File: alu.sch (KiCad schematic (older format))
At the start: 124 parts, among them U1 C96ABC, U10 74LS32, U11 74LS86, U12 74LS86, U13 74LS283, U14 74LS283, U15 74LS253, U16 74LS253, U17 74LS253, U18 74LS253, U2 74ACT04, U3 74ACT04, U4 74ACT158, U5 74ACT158, U6 74ACT158, U7 74LS08, U8 74LS08, U9 74LS32

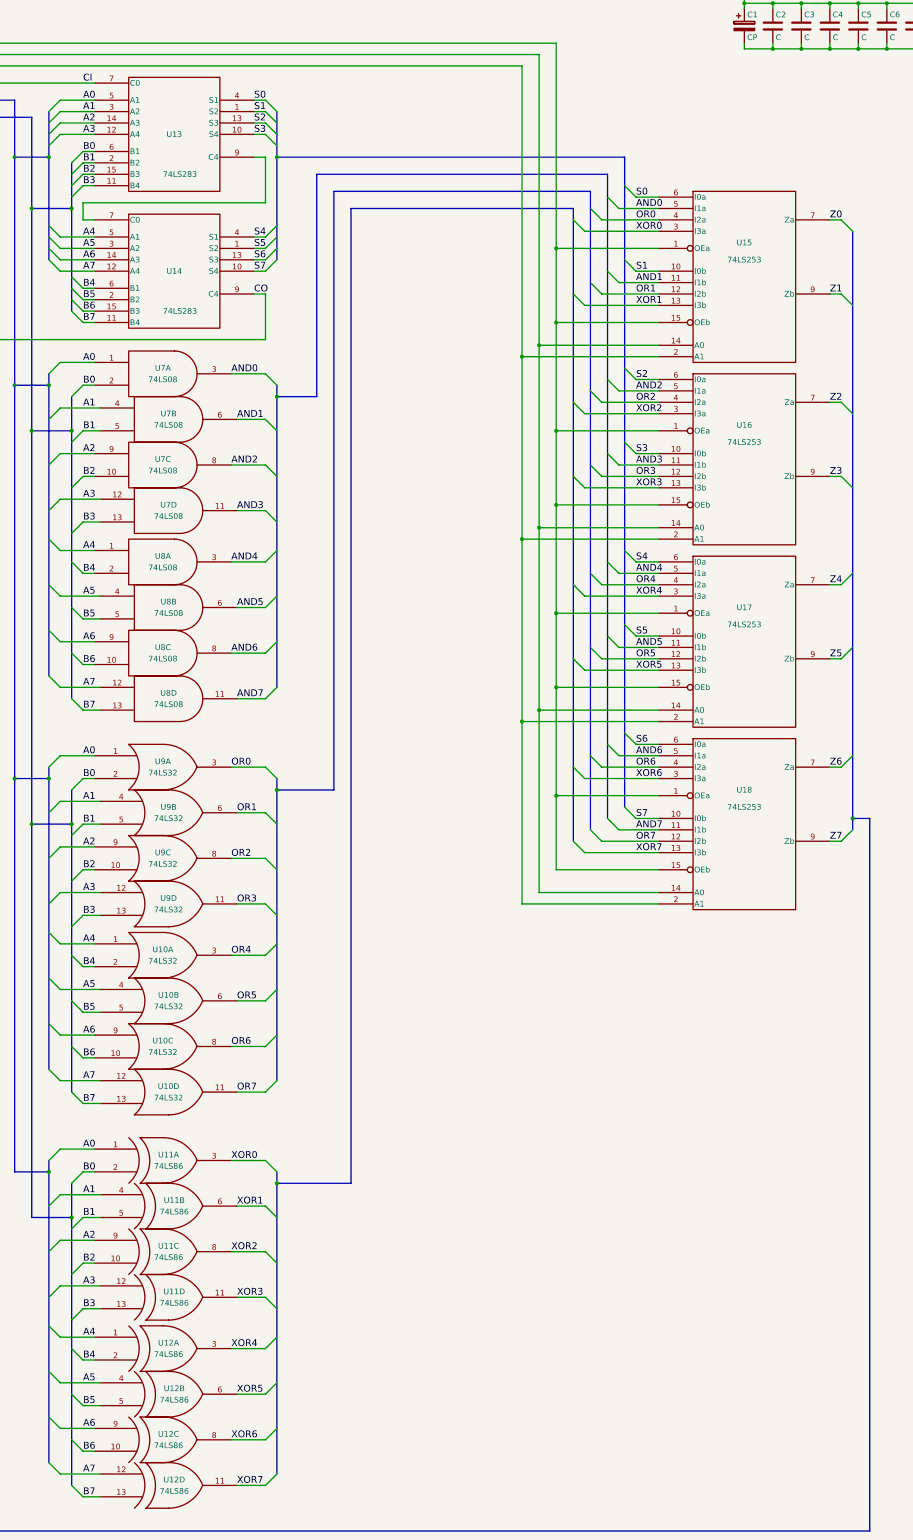
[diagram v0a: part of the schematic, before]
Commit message: component placement
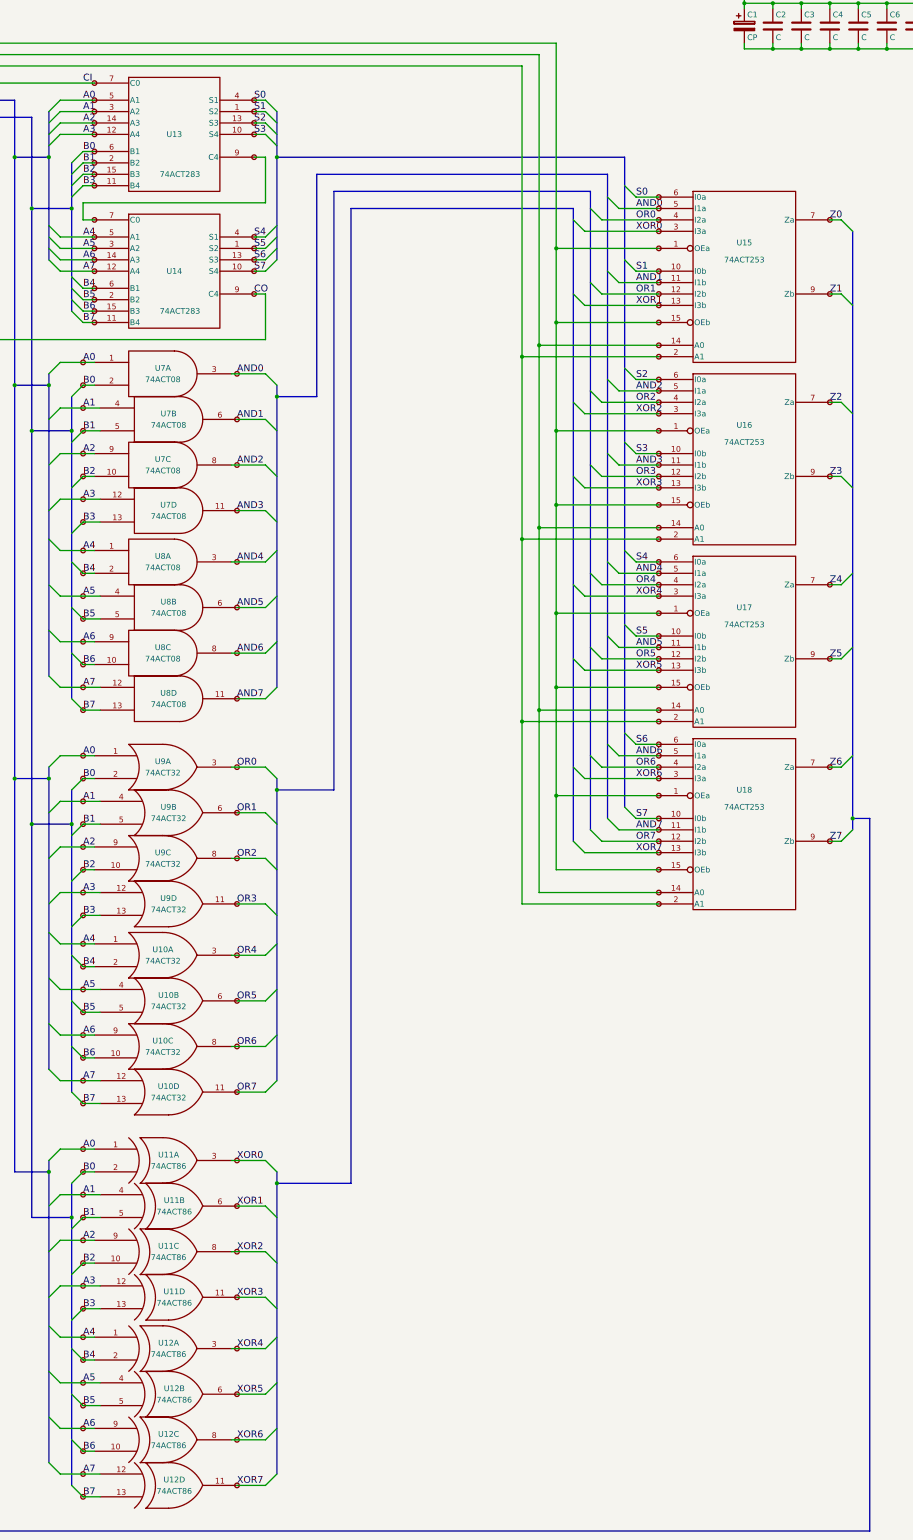
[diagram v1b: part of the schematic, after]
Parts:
- added LED100, LED101, LED102, LED103, LED104, LED105, LED106, LED107, LED108, LED109, LED110, LED111, LED112, LED113, LED114, LED115, LED116, LED117, LED118, LED119, LED120, LED121, LED122, LED123, LED124, LED125, LED126, LED127, LED128, LED129, LED130, LED131, LED132, LED133, LED134, LED135, LED136, LED137, LED138, LED139, LED140, LED141, LED142, LED143, LED144, LED145, LED146, LED147, LED148, LED149, LED150, LED151, LED152, LED153, LED154, LED155, LED156, LED157, LED158, LED159, LED160, LED161, LED162, LED163, LED164, LED165, LED166, LED167, LED168, LED169, LED170, LED171, LED172, LED173, LED174, LED175, LED176, LED177, LED178, LED179, LED180, LED181, LED182, LED183, LED184, LED185, LED186, LED187, LED188, LED189, LED190, LED191, LED192, LED193, LED194, LED195, LED196, LED197, LED198, LED199, LED200, LED201, LED202, LED203, LED204, LED205, LED206, LED207, LED208, LED209, LED210, LED211, LED212, LED213, LED214, LED215, LED216, LED217, LED218, LED219, LED220, LED221, LED222, LED223, LED224, LED225, LED226, LED227, LED228, LED229, LED230, LED231, LED232, LED233, LED234, LED235, LED236, LED237, LED238, LED239, LED240, LED241, LED242, LED243, LED244, LED89, LED90, LED91, LED92, LED93, LED94, LED95, LED96, LED97, LED98, LED99: DEBUG_LED, LEDs:LED-3MM, symbol DEBUG_LED
- U10, U9: value 74LS32 -> 74ACT32
- U11, U12: value 74LS86 -> 74ACT86
- U13, U14: value 74LS283 -> 74ACT283
- U15, U16, U17, U18: value 74LS253 -> 74ACT253
- U7, U8: value 74LS08 -> 74ACT08
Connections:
- net A0: now also LED113.2, LED137.2, LED162.2, LED89.2
- net A1: now also LED115.2, LED139.2, LED163.2, LED91.2
- net A2: now also LED117.2, LED141.2, LED164.2, LED93.2
- net A3: now also LED119.2, LED143.2, LED165.2, LED95.2
- net A4: now also LED121.2, LED145.2, LED171.2, LED97.2
- net A5: now also LED123.2, LED147.2, LED172.2, LED99.2
- net A6: now also LED101.2, LED125.2, LED149.2, LED173.2
- net A7: now also LED103.2, LED127.2, LED151.2, LED174.2
- net AND0: now also LED105.2, LED190.2
- net AND1: now also LED106.2, LED195.2
- net AND2: now also LED107.2, LED202.2
- net AND3: now also LED108.2, LED207.2
- net AND4: now also LED109.2, LED214.2
- net AND5: now also LED110.2, LED219.2
- net AND6: now also LED111.2, LED226.2
- net AND7: now also LED112.2, LED231.2
- net B0: now also LED114.2, LED138.2, LED166.2, LED90.2
- net B1: now also LED116.2, LED140.2, LED167.2, LED92.2
- net B2: now also LED118.2, LED142.2, LED168.2, LED94.2
- net B3: now also LED120.2, LED144.2, LED169.2, LED96.2
- net B4: now also LED122.2, LED146.2, LED175.2, LED98.2
- net B5: now also LED100.2, LED124.2, LED148.2, LED176.2
- net B6: now also LED102.2, LED126.2, LED150.2, LED177.2
- net B7: now also LED104.2, LED128.2, LED152.2, LED178.2
- net CI: now also LED161.2
- net CO: now also LED188.2
- net GND: now also LED100.1 (GND), LED101.1 (GND), LED102.1 (GND), LED103.1 (GND), LED104.1 (GND), LED105.1 (GND), LED106.1 (GND), LED107.1 (GND), LED108.1 (GND), LED109.1 (GND), LED110.1 (GND), LED111.1 (GND), LED112.1 (GND), LED113.1 (GND), LED114.1 (GND), LED115.1 (GND), LED116.1 (GND), LED117.1 (GND), LED118.1 (GND), LED119.1 (GND), LED120.1 (GND), LED121.1 (GND), LED122.1 (GND), LED123.1 (GND), LED124.1 (GND), LED125.1 (GND), LED126.1 (GND), LED127.1 (GND), LED128.1 (GND), LED129.1 (GND), LED130.1 (GND), LED131.1 (GND), LED132.1 (GND), LED133.1 (GND), LED134.1 (GND), LED135.1 (GND), LED136.1 (GND), LED137.1 (GND), LED138.1 (GND), LED139.1 (GND), LED140.1 (GND), LED141.1 (GND), LED142.1 (GND), LED143.1 (GND), LED144.1 (GND), LED145.1 (GND), LED146.1 (GND), LED147.1 (GND), LED148.1 (GND), LED149.1 (GND), LED150.1 (GND), LED151.1 (GND), LED152.1 (GND), LED153.1 (GND), LED154.1 (GND), LED155.1 (GND), LED156.1 (GND), LED157.1 (GND), LED158.1 (GND), LED159.1 (GND), LED160.1 (GND), LED161.1 (GND), LED162.1 (GND), LED163.1 (GND), LED164.1 (GND), LED165.1 (GND), LED166.1 (GND), LED167.1 (GND), LED168.1 (GND), LED169.1 (GND), LED170.1 (GND), LED171.1 (GND), LED172.1 (GND), LED173.1 (GND), LED174.1 (GND), LED175.1 (GND), LED176.1 (GND), LED177.1 (GND), LED178.1 (GND), LED179.1 (GND), LED180.1 (GND), LED181.1 (GND), LED182.1 (GND), LED183.1 (GND), LED184.1 (GND), LED185.1 (GND), LED186.1 (GND), LED187.1 (GND), LED188.1 (GND), LED189.1 (GND), LED190.1 (GND), LED191.1 (GND), LED192.1 (GND), LED193.1 (GND), LED194.1 (GND), LED195.1 (GND), LED196.1 (GND), LED197.1 (GND), LED198.1 (GND), LED199.1 (GND), LED200.1 (GND), LED201.1 (GND), LED202.1 (GND), LED203.1 (GND), LED204.1 (GND), LED205.1 (GND), LED206.1 (GND), LED207.1 (GND), LED208.1 (GND), LED209.1 (GND), LED210.1 (GND), LED211.1 (GND), LED212.1 (GND), LED213.1 (GND), LED214.1 (GND), LED215.1 (GND), LED216.1 (GND), LED217.1 (GND), LED218.1 (GND), LED219.1 (GND), LED220.1 (GND), LED221.1 (GND), LED222.1 (GND), LED223.1 (GND), LED224.1 (GND), LED225.1 (GND), LED226.1 (GND), LED227.1 (GND), LED228.1 (GND), LED229.1 (GND), LED230.1 (GND), LED231.1 (GND), LED232.1 (GND), LED233.1 (GND), LED234.1 (GND), LED235.1 (GND), LED236.1 (GND), LED237.1 (GND), LED238.1 (GND), LED239.1 (GND), LED240.1 (GND), LED241.1 (GND), LED242.1 (GND), LED243.1 (GND), LED244.1 (GND), LED89.1 (GND), LED90.1 (GND), LED91.1 (GND), LED92.1 (GND), LED93.1 (GND), LED94.1 (GND), LED95.1 (GND), LED96.1 (GND), LED97.1 (GND), LED98.1 (GND), LED99.1 (GND)
- net OR0: now also LED129.2, LED191.2
- net OR1: now also LED130.2, LED196.2
- net OR2: now also LED131.2, LED203.2
- net OR3: now also LED132.2, LED208.2
- net OR4: now also LED133.2, LED215.2
- net OR5: now also LED134.2, LED220.2
- net OR6: now also LED135.2, LED227.2
- net OR7: now also LED136.2, LED232.2
- net S0: now also LED179.2, LED189.2
- net S1: now also LED180.2, LED194.2
- net S2: now also LED181.2, LED201.2
- net S3: now also LED182.2, LED206.2
- net S4: now also LED184.2, LED213.2
- net S5: now also LED185.2, LED218.2
- net S6: now also LED186.2, LED225.2
- net S7: now also LED187.2, LED230.2
- net XOR0: now also LED153.2, LED192.2
- net XOR1: now also LED154.2, LED197.2
- net XOR2: now also LED155.2, LED204.2
- net XOR3: now also LED156.2, LED209.2
- net XOR4: now also LED157.2, LED216.2
- net XOR5: now also LED158.2, LED221.2
- net XOR6: now also LED159.2, LED228.2
- net XOR7: now also LED160.2, LED233.2
- net Y0: now also LED199.2, LED211.2, LED223.2, LED235.2
- net Y1: now also LED200.2, LED212.2, LED224.2, LED236.2
- net Z0: now also LED237.2
- net Z1: now also LED238.2
- net Z2: now also LED239.2
- net Z3: now also LED240.2
- net Z4: now also LED241.2
- net Z5: now also LED242.2
- net Z6: now also LED243.2
- net Z7: now also LED244.2
- net ~OE: now also LED193.2, LED198.2, LED205.2, LED210.2, LED217.2, LED222.2, LED229.2, LED234.2
- net at U13.9 (C4), U14.7 (C0): now also LED170.2, LED183.2

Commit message: pcb routing
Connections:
- net A0: now also U1.C26 (26C); no longer U1.C27 (27C)
- net A1: now also U1.C25 (25C); no longer U1.C26 (26C)
- net A2: now also U1.C24 (24C); no longer U1.C25 (25C)
- net A3: now also U1.C23 (23C); no longer U1.C24 (24C)
- net A4: now also U1.C22 (22C); no longer U1.C23 (23C)
- net A5: now also U1.C21 (21C); no longer U1.C22 (22C)
- net A6: now also U1.C20 (20C); no longer U1.C21 (21C)
- net A7: now also U1.C19 (19C); no longer U1.C20 (20C)
- net BFF: now also U1.B27 (27B); no longer U1.B28 (28B)
- net BX0: now also U1.C18 (18C); no longer U1.C19 (19C)
- net BX1: now also U1.C17 (17C); no longer U1.C18 (18C)
- net BX2: now also U1.C16 (16C); no longer U1.C17 (17C)
- net BX3: now also U1.C15 (15C); no longer U1.C16 (16C)
- net BX4: now also U1.C14 (14C); no longer U1.C15 (15C)
- net BX5: now also U1.C13 (13C); no longer U1.C14 (14C)
- net BX6: now also U1.C12 (12C); no longer U1.C13 (13C)
- net BX7: now also U1.C11 (11C); no longer U1.C12 (12C)
- net CIX: now also U1.C10 (10C); no longer U1.C11 (11C)
- net COX: now also U1.C1 (1C); no longer U1.C2 (2C)
- net CSET: now also U1.B28 (28B); no longer U1.B29 (29B)
- net GND: now also U1.A31 (31A), U1.B31 (31B), U1.C31 (31C); no longer U1.A1 (1A), U1.B1 (1B), U1.C1 (1C)
- net Y0: now also U1.C29 (29C); no longer U1.C30 (30C)
- net Y1: now also U1.C28 (28C); no longer U1.C29 (29C)
- net Z0: now also U1.C9 (9C); no longer U1.C10 (10C)
- net Z1: now also U1.C8 (8C); no longer U1.C9 (9C)
- net Z2: now also U1.C7 (7C); no longer U1.C8 (8C)
- net Z3: now also U1.C6 (6C); no longer U1.C7 (7C)
- net Z4: now also U1.C5 (5C); no longer U1.C6 (6C)
- net Z5: now also U1.C4 (4C); no longer U1.C5 (5C)
- net Z6: now also U1.C3 (3C); no longer U1.C4 (4C)
- net Z7: now also U1.C2 (2C); no longer U1.C3 (3C)
- net ~INV: now also U1.C27 (27C); no longer U1.C28 (28C)
- net ~OE: now also U1.C30 (30C); no longer U1.C31 (31C)
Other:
- moved on the sheet: U1
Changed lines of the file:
@@
 L C96ABC U1
 U 1 1 57E75D13
-P 3900 6600
-F 0 "U1" H 3900 11500 50  0000 C CNN
-F 1 "C96ABC" V 4150 6600 50  0000 C CNN
-F 2 "Mechanical_Sockets:Socket_DIN41612-CaseC1-full-Male-96Pin-3rows" H 3900 6600 50  0001 C CNN
-F 3 "" H 3900 6600 50  0000 C CNN
-	1    3900 6600
+P 3900 6300
+F 0 "U1" H 3900 11200 50  0000 C CNN
+F 1 "C96ABC" V 4150 6300 50  0000 C CNN
+F 2 "Mechanical_Sockets:Socket_DIN41612-CaseC1-full-Male-96Pin-3rows" H 3900 6300 50  0001 C CNN
+F 3 "" H 3900 6300 50  0000 C CNN
+	1    3900 6300
 	-1   0    0    1
 $EndComp
@@
 L VCC #PWR01
 U 1 1 57E80CD3
-P 4500 1650
-F 0 "#PWR01" H 4500 1500 50  0001 C CNN
-F 1 "VCC" H 4500 1800 50  0000 C CNN
-F 2 "" H 4500 1650 50  0000 C CNN
-F 3 "" H 4500 1650 50  0000 C CNN
-	1    4500 1650
+P 4500 1350
+F 0 "#PWR01" H 4500 1200 50  0001 C CNN
+F 1 "VCC" H 4500 1500 50  0000 C CNN
+F 2 "" H 4500 1350 50  0000 C CNN
+F 3 "" H 4500 1350 50  0000 C CNN
+	1    4500 1350
 	1    0    0    -1
 $EndComp
@@
 L GND #PWR02
 U 1 1 57E812B2
-P 4500 11650
-F 0 "#PWR02" H 4500 11400 50  0001 C CNN
-F 1 "GND" H 4500 11500 50  0000 C CNN
-F 2 "" H 4500 11650 50  0000 C CNN
-F 3 "" H 4500 11650 50  0000 C CNN
-	1    4500 11650
-	1    0    0    -1
+P 4800 1300
+F 0 "#PWR02" H 4800 1050 50  0001 C CNN
+F 1 "GND" H 4800 1150 50  0000 C CNN
+F 2 "" H 4800 1300 50  0000 C CNN
+F 3 "" H 4800 1300 50  0000 C CNN
+	1    4800 1300
+	-1   0    0    -1
 $EndComp
 $Comp
@@
 L PWR_FLAG #FLG04
 U 1 1 57E9C81D
-P 4450 1700
-F 0 "#FLG04" H 4450 1795 50  0001 C CNN
-F 1 "PWR_FLAG" V 4550 2000 50  0000 C CNN
-F 2 "" H 4450 1700 50  0000 C CNN
-F 3 "" H 4450 1700 50  0000 C CNN
-	1    4450 1700
+P 4450 1400
+F 0 "#FLG04" H 4450 1495 50  0001 C CNN
+F 1 "PWR_FLAG" V 4550 1700 50  0000 C CNN
+F 2 "" H 4450 1400 50  0000 C CNN
+F 3 "" H 4450 1400 50  0000 C CNN
+	1    4450 1400
 	0    -1   -1   0
 $EndComp
@@
 L PWR_FLAG #FLG05
 U 1 1 57E410D7
-P 4450 11600
-F 0 "#FLG05" H 4450 11695 50  0001 C CNN
-F 1 "PWR_FLAG" V 4550 11900 50  0000 C CNN
-F 2 "" H 4450 11600 50  0000 C CNN
-F 3 "" H 4450 11600 50  0000 C CNN
-	1    4450 11600
-	0    -1   -1   0
+P 4850 1250
+F 0 "#FLG05" H 4850 1345 50  0001 C CNN
+F 1 "PWR_FLAG" V 4950 1550 50  0000 C CNN
+F 2 "" H 4850 1250 50  0000 C CNN
+F 3 "" H 4850 1250 50  0000 C CNN
+	1    4850 1250
+	0    1    -1   0
 $EndComp
 Wire Wire Line
@@
 	4650 2150 4400 2150
 Wire Wire Line
-	4500 1850 4400 1850
-Wire Wire Line
-	4500 1650 4500 2050
-Wire Wire Line
-	4500 1950 4400 1950
-Connection ~ 4500 1850
-Wire Wire Line
-	4500 2050 4400 2050
-Connection ~ 4500 1950
+	4500 1550 4400 1550
 Wire Wire Line
-	4400 11150 4500 11150
+	4500 1350 4500 1750
 Wire Wire Line
-	4500 11150 4500 11650
+	4500 1650 4400 1650
+Connection ~ 4500 1550
 Wire Wire Line
-	4400 11250 4500 11250
-Connection ~ 4500 11250
+	4500 1750 4400 1750
+Connection ~ 4500 1650
 Wire Wire Line
-	4400 11350 4500 11350
-Connection ~ 4500 11350
+	4800 1250 4800 1300
 Wire Wire Line
 	5650 5850 6250 5850
@@
 Connection ~ 7650 9550
 Wire Wire Line
-	4450 1700 4500 1700
-Connection ~ 4500 1700
+	4450 1400 4500 1400
+Connection ~ 4500 1400
 Wire Wire Line
 	8000 10100 7650 10100
@@
 Connection ~ 7650 10450
 Wire Wire Line
-	4500 11600 4450 11600
-Connection ~ 4500 11600
+	4550 1250 4850 1250
+Connection ~ 4800 1250
 $Comp
 L C C9
@@
 	1    0    0    -1
 $EndComp
+Wire Wire Line
+	4400 1950 4550 1950
+Wire Wire Line
+	4550 1250 4550 2050
+Wire Wire Line
+	4400 1850 4550 1850
+Connection ~ 4550 1850
+Wire Wire Line
+	4550 2050 4400 2050
+Connection ~ 4550 1950
 $EndSCHEMATC
